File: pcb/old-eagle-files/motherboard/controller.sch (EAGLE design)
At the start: 89 parts, among them J1 SNG-2MM-HEADER-04-V, J10 SNG-100-HEADER-01-HDR-V, J11 SNG-100-HEADER-01-HDR-V, J2 DL-1.25MM-HEADER-20, J3 MICRO_SD, J5 7498011122R, J6 USB_A, J7 DL-1.25MM-HEADER-10, J8 CUI-PJ-013C, J9 SNG-100-HEADER-01-HDR-V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

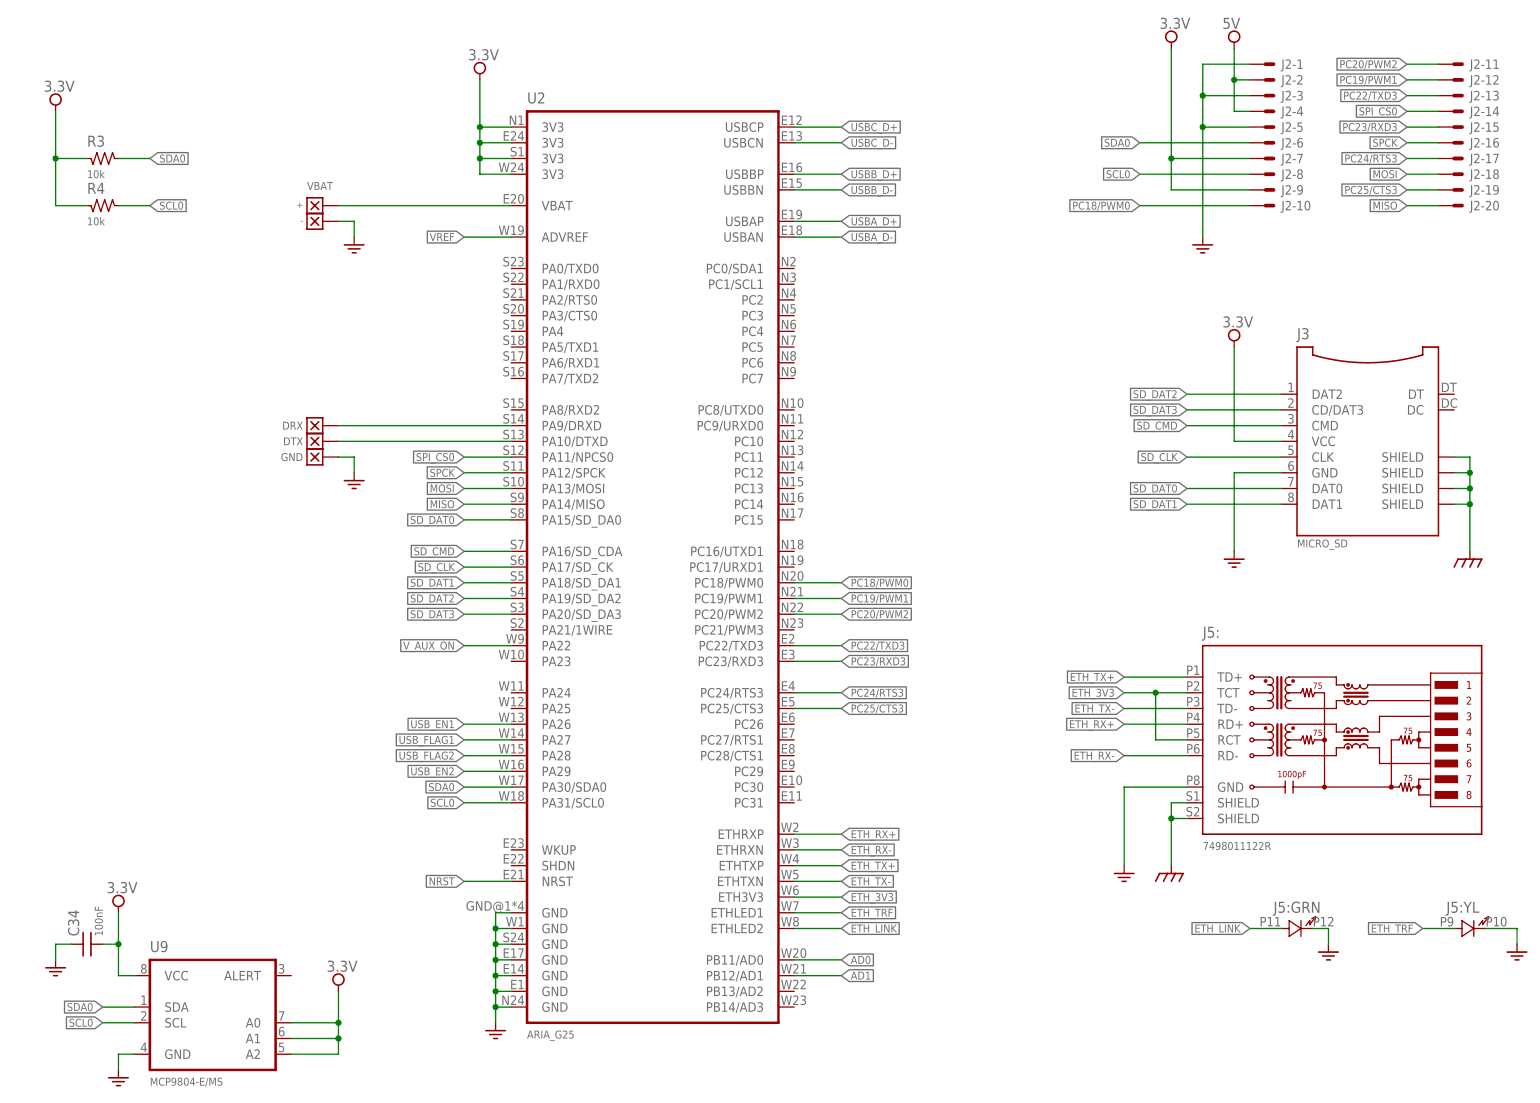
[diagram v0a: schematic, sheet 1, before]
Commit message: Converted motherboard and left-panel project files to Kicad
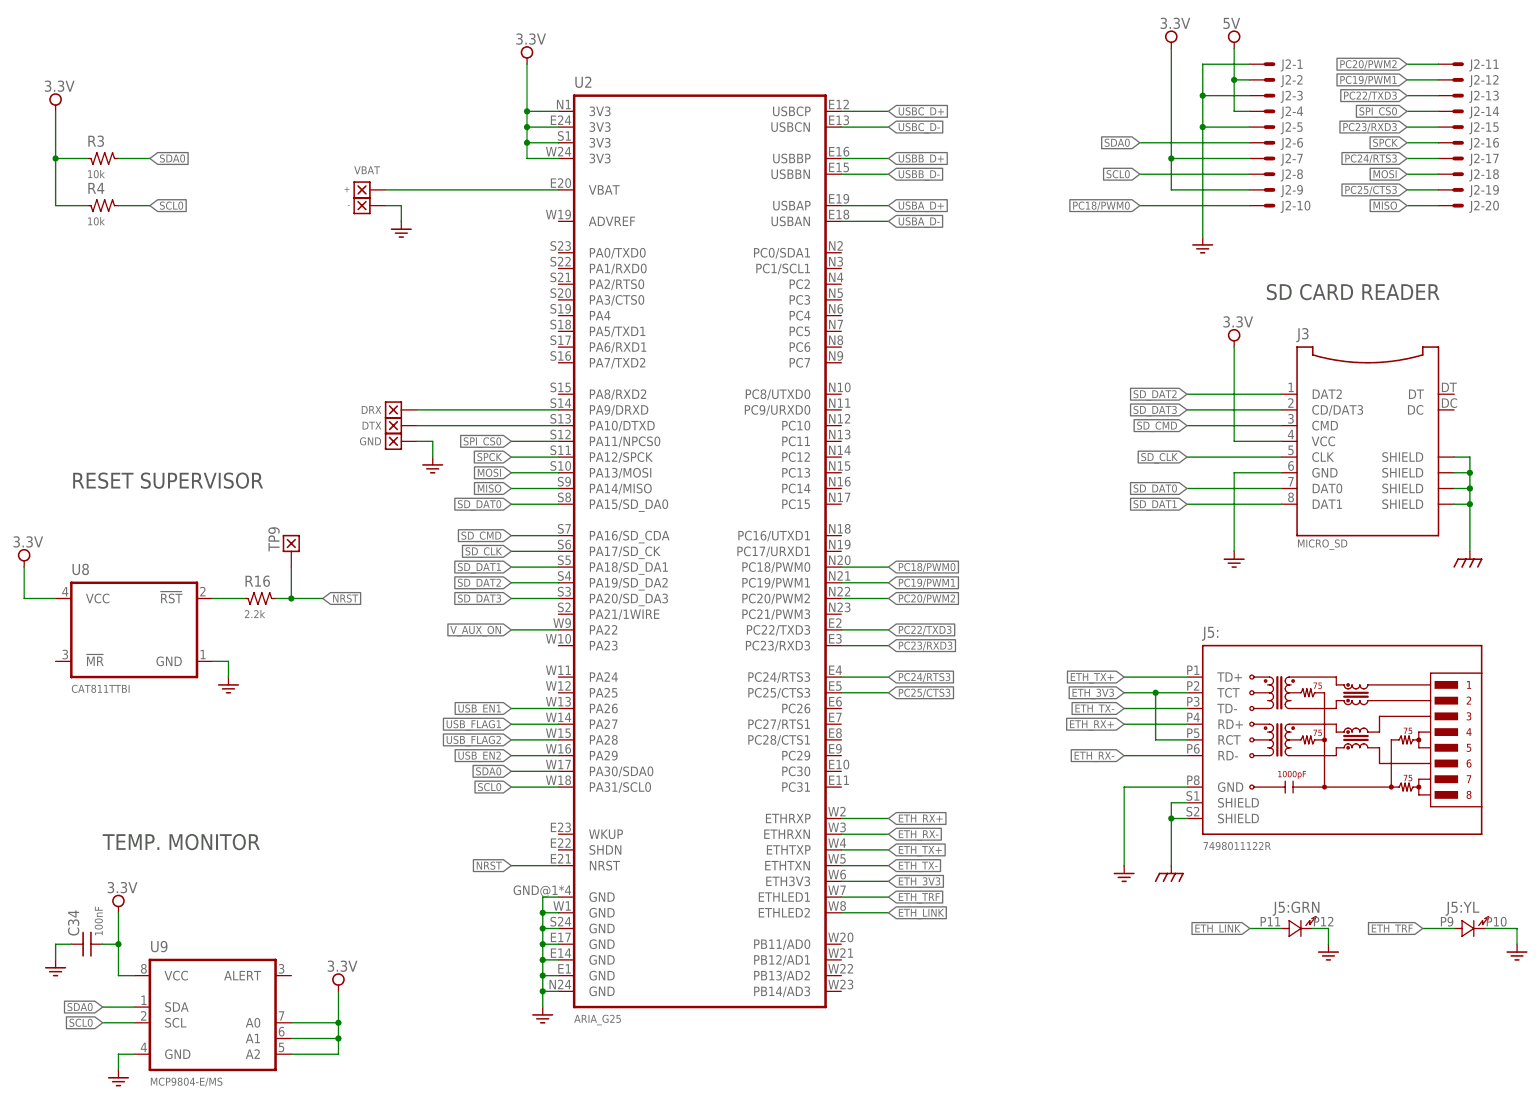
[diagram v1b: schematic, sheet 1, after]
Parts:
- removed J11: SNG-100-HEADER-01-HDR-V, Connectors:SNG-100-HEADER-01-HDR-V
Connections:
- removed net AD0: U2.PB11/AD0
- removed net AD1: U2.PB12/AD1
- removed net VREF: U2.ADVREF
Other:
- note added: "SD CARD READER"
- note added: "TEMP. MONITOR"
- moved on the sheet: U2
